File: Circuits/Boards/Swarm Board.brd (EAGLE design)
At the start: 76.2 x 76.2 mm, 95 parts, among them CON1 ISP(2X3), T1 NPN2N2222, T10 TEFT4300, T11 NPN2N2222, T12 NPN2N2222, T13 NPN2N2222, T14 NPN2N2222, T15 NPN2N2222, T16 NPN2N2222, T17 NPN2N2222, T18 NPN2N2222, T2 NPN2N2222, T3 NPN2N2222, T4 TEFT4300, T5 TEFT4300, T6 TEFT4300, T7 TEFT4300, T8 TEFT4300, T9 TEFT4300, U1 ATMEGA324P, U2 MCP73832SOT-23, U3 TB6552FN/FNG

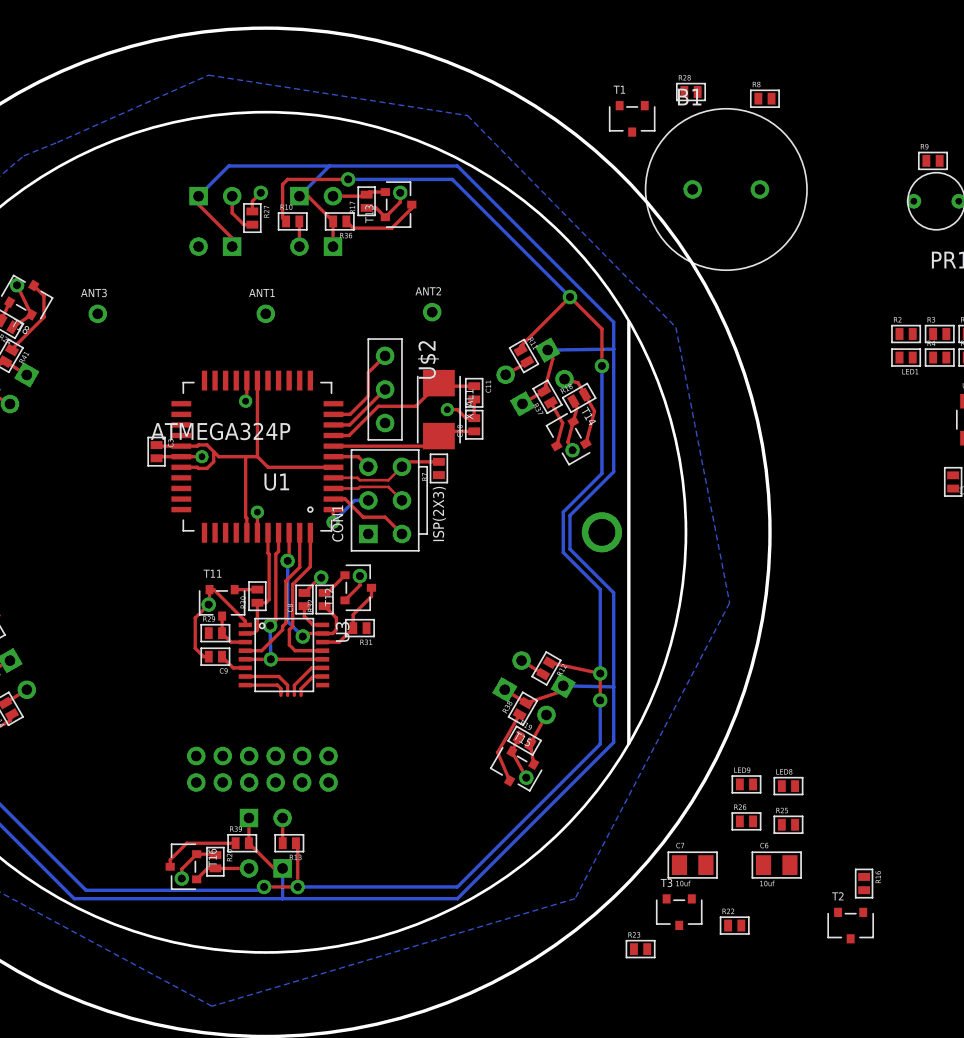
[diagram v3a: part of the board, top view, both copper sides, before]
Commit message: 
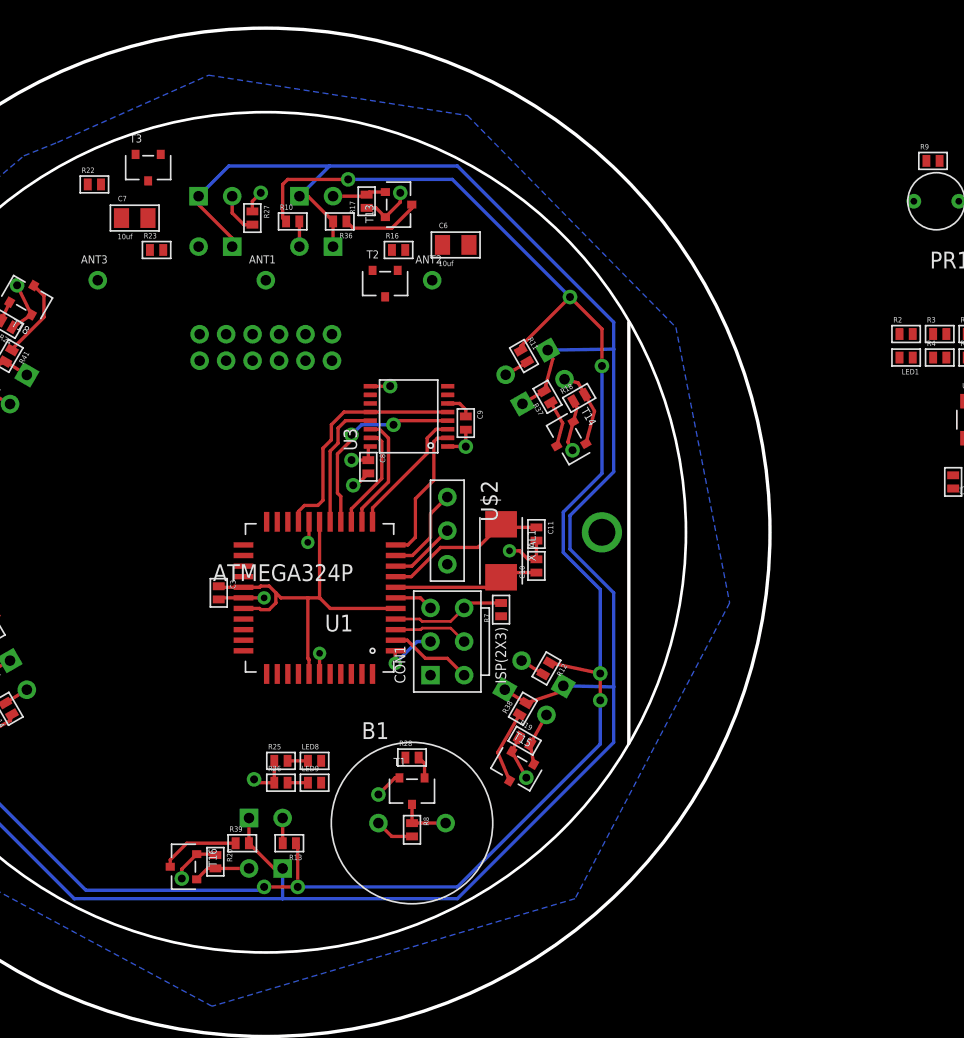
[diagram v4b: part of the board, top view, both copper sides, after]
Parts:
- removed R29, R31: 10k, Passive:0603
- removed R30, R32: 1k, Passive:0603
- removed T11, T12: NPN2N2222, Passive:SOT23
- moved R22 74.0 mm to (18.8, 58.0)
- moved T3 69.1 mm to (22.9, 59.3)
- moved C7 64.6 mm to (21.8, 55.5)
- moved R23 64.3 mm to (23.5, 53.1)
- moved R8 61.3 mm to (42.8, 9.27), turned to 270 degrees
- moved T2 59.9 mm to (40.8, 50.5)
- moved R16 59.4 mm to (41.8, 53.1), turned to 0 degrees
- moved R28 54.5 mm to (42.8, 14.7)
- moved T1 53.5 mm to (42.8, 12.2)
- moved B1 53.4 mm to (42.8, 9.78)
- moved C6 52.8 mm to (46.1, 53.5)
- moved R25 38.7 mm to (32.9, 14.5)
- moved LED8 35.9 mm to (35.4, 14.5)
- moved R26 35.3 mm to (32.9, 12.8)
- moved LED9 32.6 mm to (35.4, 12.8)
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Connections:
- removed net AIN: R30.1, U1.40, U3.2
- removed net BIN: R32.1, U1.42, U3.15
- removed net N$22: R30.2, T11.1
- removed net N$28: R36.1, T13.3
- removed net N$29: R37.1, T14.3
- removed net N$30: R38.1, T15.3
- removed net N$31: R39.1, T16.3
- removed net N$32: R40.1, T17.3
- removed net N$33: R41.1, T18.3
- removed net N$7: R32.2, T12.1
- new net AIN1: U1.11, U3.2
- new net BIN1: U1.14, U3.15
- new net RX1: R36.1, T13.3, U1.21
- new net RX2: R37.1, T14.3, U1.22
- new net RX3: R38.1, T15.3, U1.23
- new net RX4: R39.1, T16.3, U1.24
- new net RX5: R40.1, T17.3, U1.25
- new net RX6: R41.1, T18.3, U1.26
- net +3V: no longer LED8.2, LED9.2, R29.1, R31.1, U$1.4
- net +VBAT: now also U$1.7; no longer U$1.3
- net AIN2: now also U1.12; no longer R29.2, T11.3
- net APWM: now also U1.15; no longer U1.43
- net BIN2: now also U1.13; no longer R31.2, T12.3
- net BPWM: now also U1.16; no longer U1.44
- net BUMPER: now also U1.34; no longer U$1.8, U1.35
- net BUZZER: now also U1.44
- net CHGDETECT: now also U1.40
- net CHGSTATUS: now also U1.41
- net DISTANCELED: now also U1.31; no longer U1.32
- net DISTANCERECEIVE: now also U1.30; no longer U1.31
- net GND: now also R25.1, R26.1, U$1.6, U$1.8; no longer T11.2, T12.2, U$1.10, U$1.9
- net IRENABLE: now also U$1.9, U1.33; no longer U$1.5, U1.34
- net LED1: now also LED8.2, U1.42; no longer R25.1
- net LED2: now also LED9.2, U1.43; no longer R26.1
- net LIGHTSENSE: now also U1.32; no longer U1.33
- net LINESENSE1: now also U1.36; no longer U$1.7, U1.37
- net LINESENSE2: now also U1.35; no longer U$1.6, U1.36
- net MA+: now also U$1.12; no longer U$1.1
- net MA-: now also U$1.11; no longer U$1.2
- net MB+: now also U$1.2; no longer U$1.12
- net MB-: now also U$1.1; no longer U$1.11
- net STBY: now also U1.19; no longer U1.41
- net TRANSMITLEDS: now also U1.20
- net VSENSE: now also U1.37; no longer U1.30
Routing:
- net BIN: track 13.3 -> 0.00 mm, vias 2 -> 0
- net AIN1: track 0.00 -> 10.7 mm
- net AIN: track 9.15 -> 0.00 mm
- net BIN1: track 0.00 -> 8.00 mm
- net AIN2: track 3.33 -> 9.86 mm
- net RX6: track 0.00 -> 6.18 mm
- net N$33: track 6.18 -> 0.00 mm
- net RX1: track 0.00 -> 6.05 mm
- net N$28: track 6.05 -> 0.00 mm
- net RX4: track 0.00 -> 5.99 mm
- net N$31: track 5.99 -> 0.00 mm
- net RX3: track 0.00 -> 5.63 mm
- net N$30: track 5.63 -> 0.00 mm
- net MA+: track 4.24 -> 0.00 mm
- net N$9: track 0.00 -> 3.96 mm
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
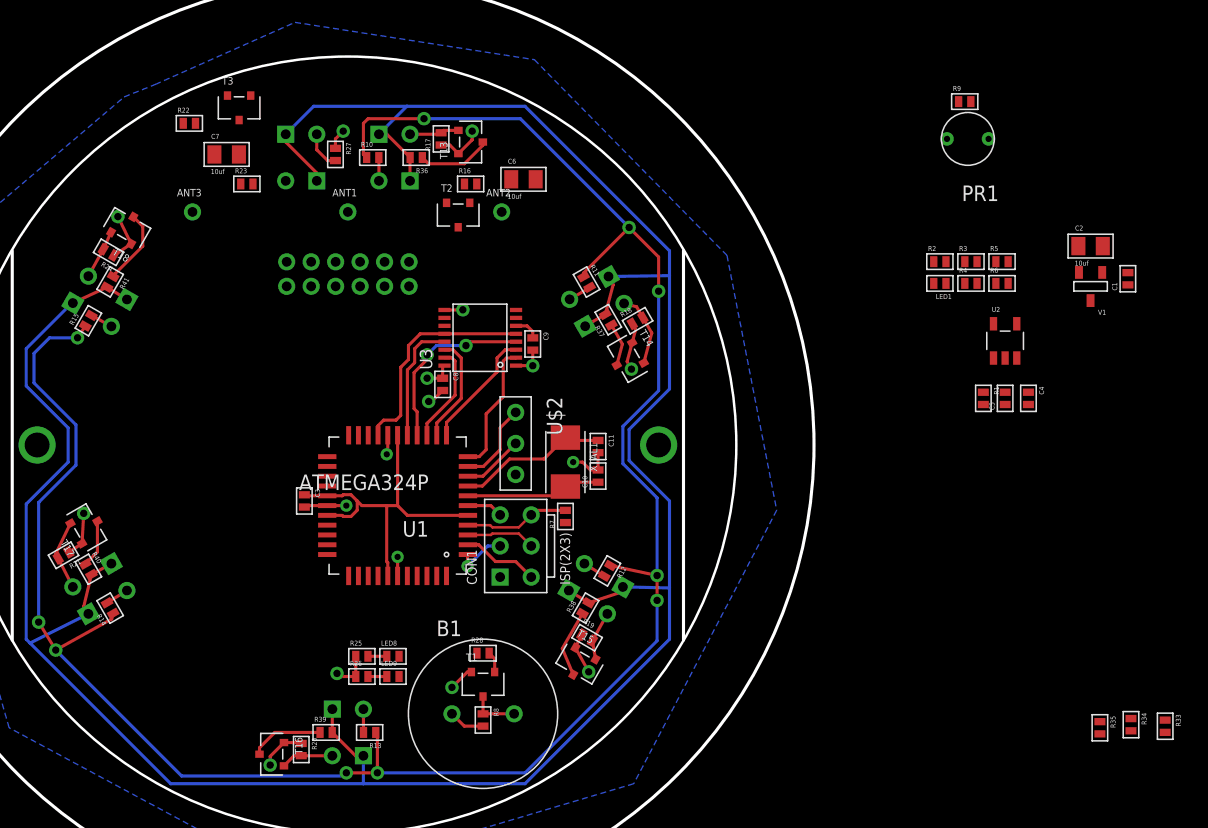
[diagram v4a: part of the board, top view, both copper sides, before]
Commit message: 
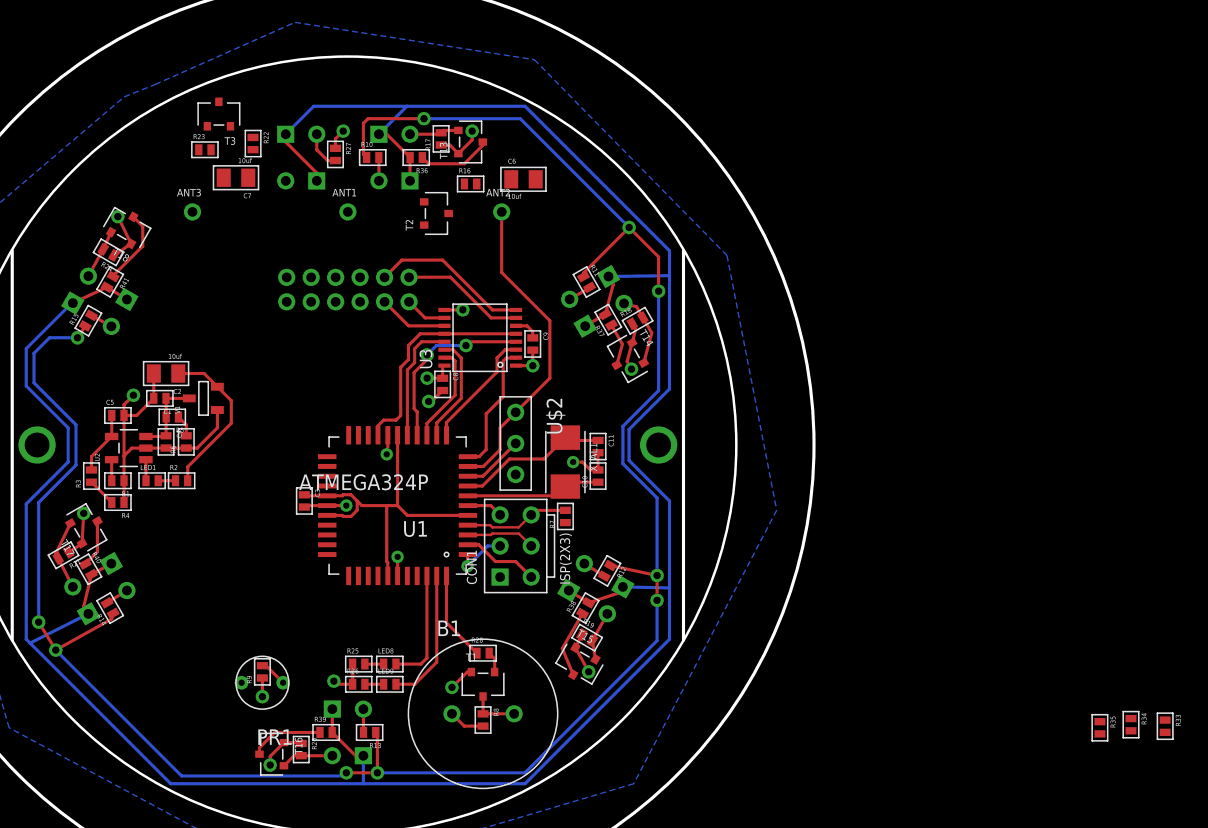
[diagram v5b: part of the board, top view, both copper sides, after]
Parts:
- moved C1 79.7 mm to (16.4, 35.6), turned to 180 degrees
- moved C2 76.3 mm to (16.9, 37.6), turned to 180 degrees
- moved R3 74.0 mm to (10.8, 29.2), turned to 90 degrees
- moved R9 73.9 mm to (24.8, 13.2), turned to 90 degrees
- moved V1 73.1 mm to (19.9, 35.6), turned to 90 degrees
- moved PR1 72.8 mm to (24.8, 12.3)
- moved C5 72.5 mm to (13.0, 34.2), turned to 0 degrees
- moved U2 72.2 mm to (13.8, 31.5), turned to 90 degrees
- moved R4 72.0 mm to (13.0, 27.1), turned to 180 degrees
- moved R1 71.1 mm to (13.0, 28.8), turned to 180 degrees
- moved C4 70.6 mm to (16.9, 32.0)
- moved R5 69.0 mm to (17.4, 34.0), turned to 180 degrees
- moved R6 67.9 mm to (18.5, 32.0), turned to 90 degrees
- moved LED1 66.4 mm to (15.7, 28.8), turned to 0 degrees
- moved R2 64.5 mm to (18.2, 28.8)
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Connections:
- net CHGDETECT: now also U1.41; no longer U1.40
- net CHGSTATUS: now also U1.40; no longer U1.41
- net GND: no longer U$1.8
- net IRENABLE: no longer U$1.9
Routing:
- net GND: track 49.3 -> 75.0 mm, vias 16 -> 18
- net DATAANTENNA: track 6.77 -> 25.9 mm
- net +3V: track 256.1 -> 269.4 mm
- net MA-: track 0.00 -> 13.0 mm
- net LED2: track 0.00 -> 11.1 mm
- net MA+: track 0.00 -> 10.1 mm
- net LED1: track 0.00 -> 9.45 mm
- net BUZZER: track 0.00 -> 7.34 mm
- net +VBAT: track 2.08 -> 8.72 mm
- net MB+: track 0.00 -> 5.71 mm
- net +VCHG: track 0.00 -> 5.14 mm
- net MB-: track 0.00 -> 3.44 mm
- net CHGDETECT: track 0.00 -> 2.35 mm
- net LIGHTSENSE: track 0.00 -> 2.27 mm
- net VSENSE: track 0.00 -> 1.80 mm
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
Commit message: Finished routing
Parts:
- moved R33 72.1 mm to (34.3, 41.4), turned to 180 degrees
- moved R35 70.7 mm to (29.8, 39.9), turned to 180 degrees
- moved R34 70.5 mm to (32.4, 39.9), turned to 0 degrees
- moved PR1 9.59 mm to (23.6, 21.8)
- moved R9 9.59 mm to (23.6, 22.7)
- moved T2 8.29 mm to (45.3, 56.0), turned to 180 degrees
- moved C7 5.73 mm to (23.0, 59.3)
- moved T3 2.90 mm to (23.0, 56.5), turned to 0 degrees
- moved LED8 2.57 mm to (34.3, 16.3)
- moved LED9 2.57 mm to (34.3, 14.6)
- moved R25 2.57 mm to (31.8, 16.3)
- moved R26 2.57 mm to (31.8, 14.6)
- moved R23 2.51 mm to (21.8, 54.1), turned to 180 degrees
- moved R22 2.50 mm to (26.2, 55.1), turned to 0 degrees
- moved V1 0.76 mm to (20.7, 35.6), turned to 270 degrees
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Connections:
- net +3V: now also U$1.8
- net BUMPER: now also U$1.5
- net GND: now also U$1.9
- net IRENABLE: now also U$1.10
- net LINESENSE1: now also U$1.3
- net LINESENSE2: now also U$1.4
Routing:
- net +3V: track 269.4 -> 375.6 mm, vias 1 -> 8
- net DISTANCERECEIVE: track 3.17 -> 52.5 mm, vias 0 -> 2
- net +VBAT: track 8.72 -> 56.4 mm
- net DISTANCELED: track 0.00 -> 43.2 mm, vias 0 -> 2
- net RX1: track 6.05 -> 44.5 mm, vias 0 -> 2
- net IRENABLE: track 0.00 -> 38.0 mm, vias 0 -> 1
- net TRANSMITLEDS: track 0.00 -> 36.8 mm, vias 0 -> 2
- net RX3: track 5.63 -> 41.7 mm, vias 0 -> 2
- net RX2: track 3.58 -> 38.2 mm, vias 0 -> 2
- net RX6: track 6.18 -> 38.5 mm, vias 0 -> 2
- net VSENSE: track 1.80 -> 34.0 mm, vias 0 -> 2
- net CHGDETECT: track 2.35 -> 33.2 mm
- net RX4: track 5.99 -> 36.7 mm, vias 0 -> 2
- net CHGSTATUS: track 1.72 -> 31.5 mm
- net +VCHG: track 5.14 -> 34.3 mm
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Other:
- board size 76.2 x 76.2 mm -> 63.5 x 63.5 mm

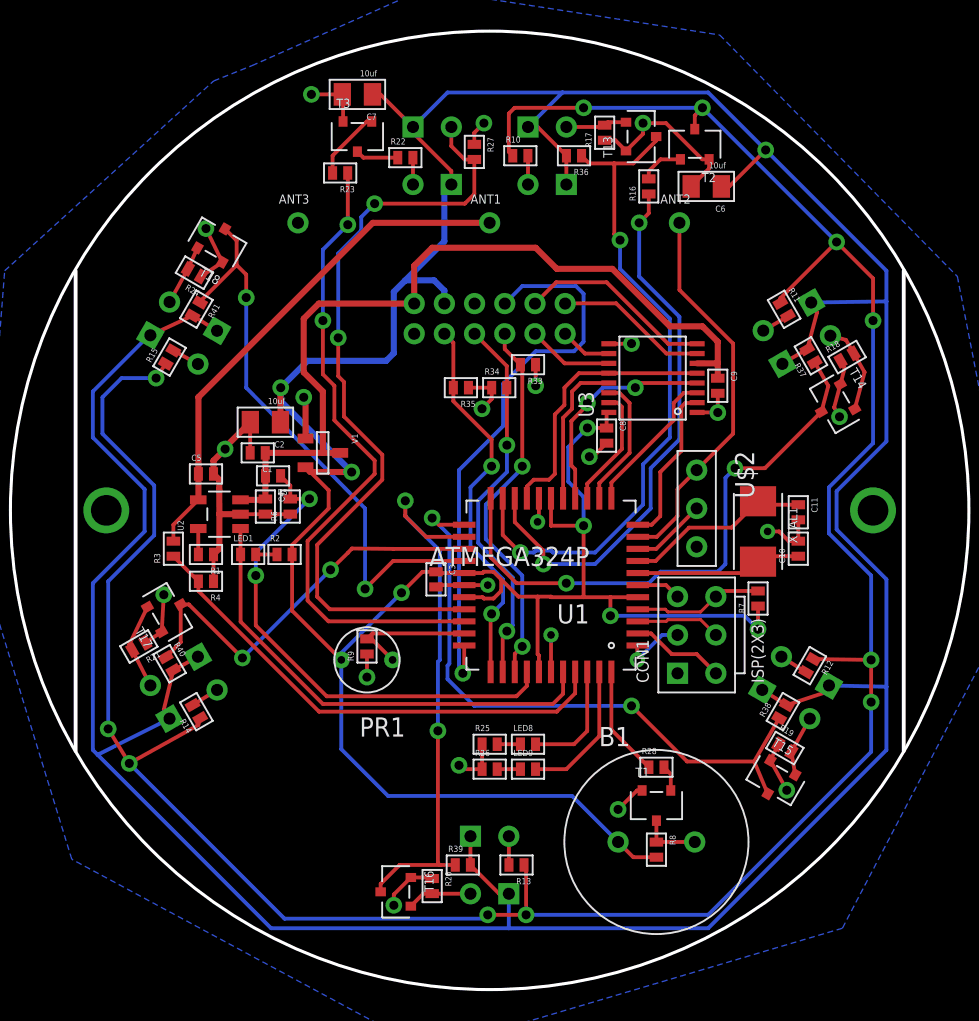
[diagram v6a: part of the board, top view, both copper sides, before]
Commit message: 
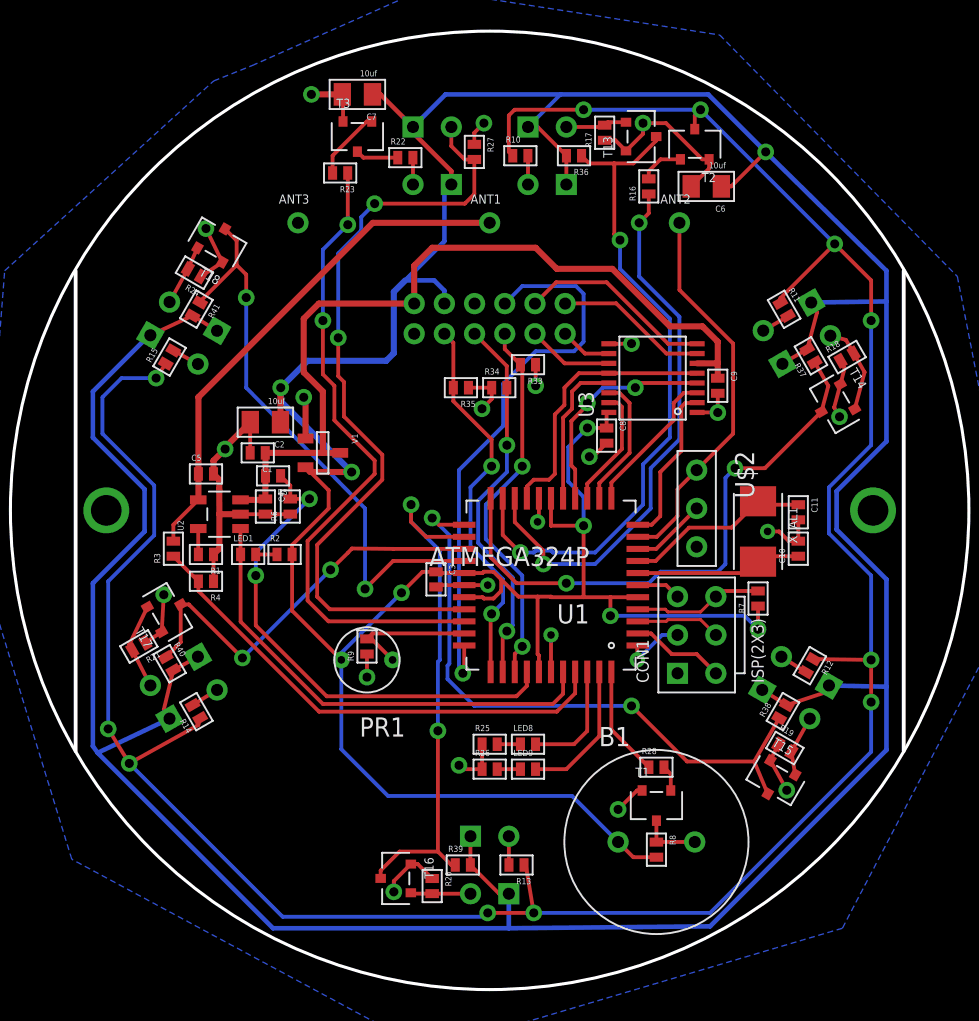
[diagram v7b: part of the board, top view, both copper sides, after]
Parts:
- moved T16 0.89 mm to (25.5, 7.37)
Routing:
- net RX4: track 36.7 -> 35.3 mm
- net N$10: track 176.2 -> 175.3 mm
- net +3V: track 375.6 -> 375.0 mm
